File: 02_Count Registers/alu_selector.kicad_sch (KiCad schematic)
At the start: 1 part, among them U11 74LS245

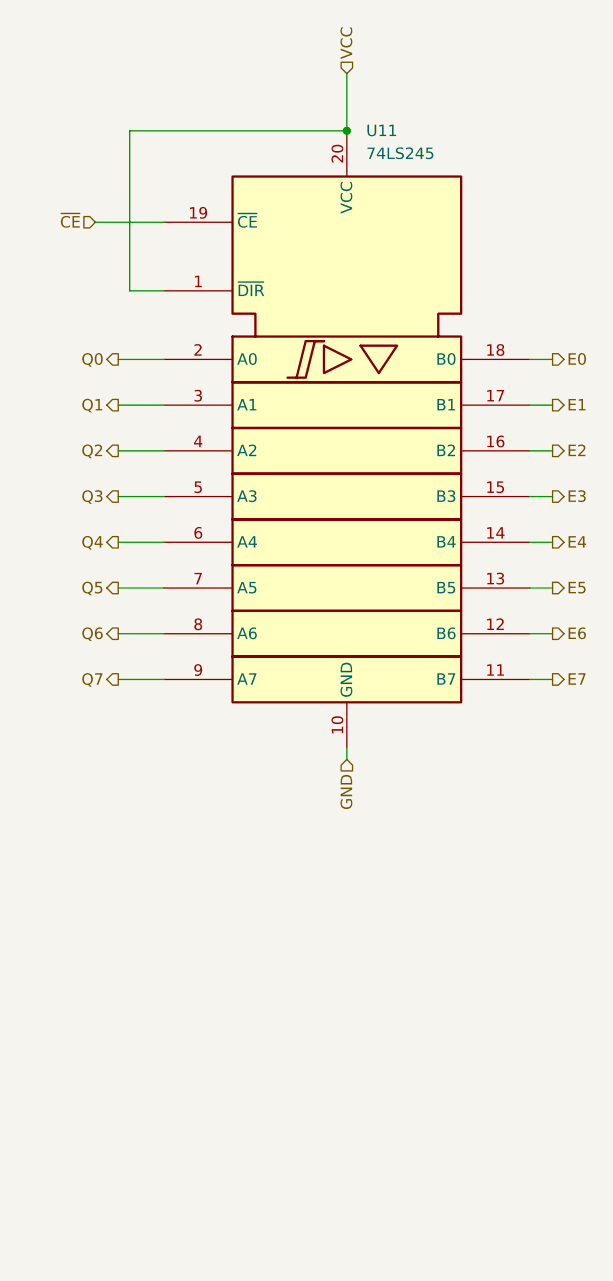
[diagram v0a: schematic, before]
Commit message: Last revision of the cpu, all boards have been ordered. Implementation to be tested and documented in following commits.
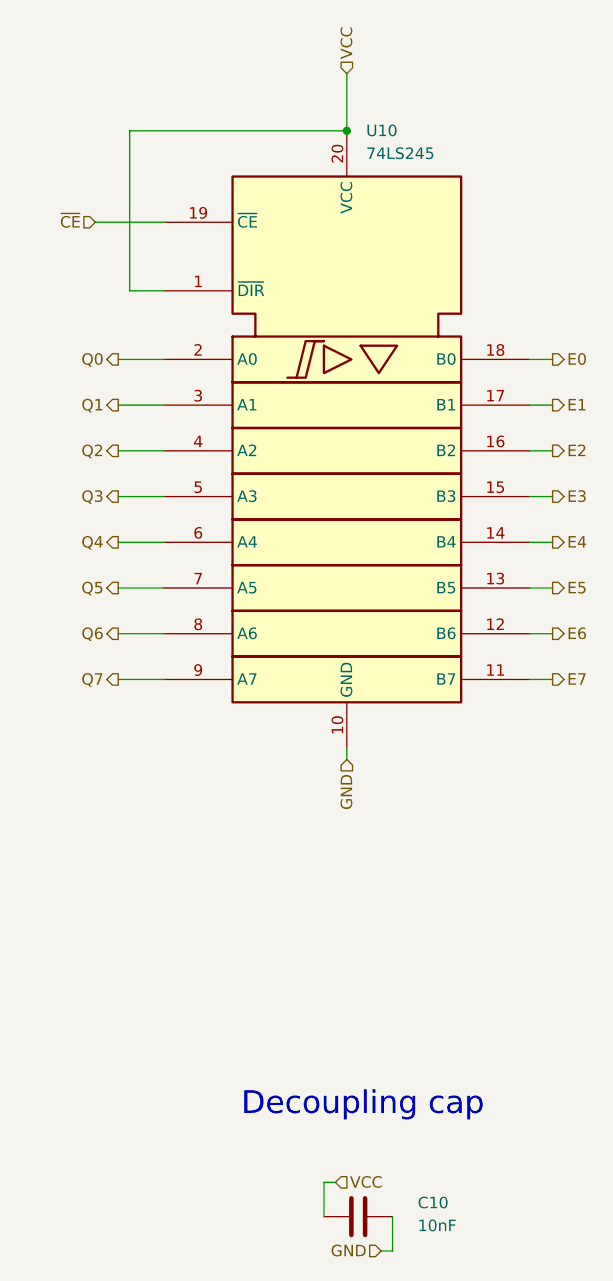
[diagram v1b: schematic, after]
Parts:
- added C10: 10nF, Capacitor_THT:C_Disc_D4.7mm_W2.5mm_P5.00mm, symbol Device:C
- renumbered U11 to U10
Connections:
- net GND: now also C10.2
- net VCC: now also C10.1
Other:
- note added: "Decoupling cap"
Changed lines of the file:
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@@
 		(company "Marco Vettigli")
+	)
+	(text "Decoupling cap"
+		(exclude_from_sim no)
+		(at 156.718 174.244 0)
+		(effects
+			(font
+				(size 2.54 2.54)
+			)
+		)
 	)
 	(junction
@@
 	(wire
 		(pts
+			(xy 160.02 190.5) (xy 160.02 186.69)
+		)
+		(stroke
+			(width 0)
+			(type default)
+		)
+	)
+	(wire
+		(pts
 			(xy 129.54 121.92) (xy 134.62 121.92)
 		)
@@
 	(wire
 		(pts
+			(xy 152.4 182.88) (xy 152.4 186.69)
+		)
+		(stroke
+			(width 0)
+			(type default)
+		)
+	)
+	(wire
+		(pts
 			(xy 129.54 91.44) (xy 134.62 91.44)
 		)
@@
 	(wire
 		(pts
+			(xy 158.75 190.5) (xy 160.02 190.5)
+		)
+		(stroke
+			(width 0)
+			(type default)
+		)
+	)
+	(wire
+		(pts
 			(xy 129.54 101.6) (xy 134.62 101.6)
 		)
@@
 	(wire
 		(pts
+			(xy 153.67 182.88) (xy 152.4 182.88)
+		)
+		(stroke
+			(width 0)
+			(type default)
+		)
+	)
+	(wire
+		(pts
 			(xy 154.94 59.69) (xy 154.94 66.04)
 		)
@@
 		)
 	)
+	(hierarchical_label "VCC"
+		(shape input)
+		(at 153.67 182.88 0)
+		(effects
+			(font
+				(size 1.27 1.27)
+			)
+			(justify left)
+		)
+	)
 	(hierarchical_label "E2"
 		(shape output)
@@
 			)
 			(justify left)
+		)
+	)
+	(hierarchical_label "GND"
+		(shape input)
+		(at 158.75 190.5 180)
+		(effects
+			(font
+				(size 1.27 1.27)
+			)
+			(justify right)
 		)
 	)
@@
 			)
 			(justify left)
+		)
+	)
+	(symbol
+		(lib_id "Device:C")
+		(at 156.21 186.69 90)
+		(unit 1)
+		(exclude_from_sim no)
+		(in_bom yes)
+		(on_board yes)
+		(dnp no)
+		(property "Reference" "C10"
+			(at 162.814 185.166 90)
+			(effects
+				(font
+					(size 1.27 1.27)
+				)
+				(justify right)
+			)
+		)
+		(property "Value" "10nF"
+			(at 162.814 187.706 90)
+			(effects
+				(font
+					(size 1.27 1.27)
+				)
+				(justify right)
+			)
+		)
+		(property "Footprint" "Capacitor_THT:C_Disc_D4.7mm_W2.5mm_P5.00mm"
+			(at 160.02 185.7248 0)
+			(effects
+				(font
+					(size 1.27 1.27)
+				)
+				(hide yes)
+			)
+		)
+		(property "Datasheet" "~"
+			(at 156.21 186.69 0)
+			(effects
+				(font
+					(size 1.27 1.27)
+				)
+				(hide yes)
+			)
+		)
+		(property "Description" "Unpolarized capacitor"
+			(at 156.21 186.69 0)
+			(effects
+				(font
+					(size 1.27 1.27)
+				)
+				(hide yes)
+			)
+		)
+		(pin "2"
+		)
+		(pin "1"
+		)
+		(instances
+			(project "Count Registers"
+				(path "/8a49c3c0-9e79-4a3c-9ae2-67e55d7fae8f/02d723ad-ab13-44db-b1f0-9a59f25d4ef1"
+					(reference "C11")
+					(unit 1)
+				)
+				(path "/8a49c3c0-9e79-4a3c-9ae2-67e55d7fae8f/56373549-06a1-42b1-826c-939e5630208c"
+					(reference "C13")
+					(unit 1)
+				)
+				(path "/8a49c3c0-9e79-4a3c-9ae2-67e55d7fae8f/5f2c1d02-b1c4-49bc-9868-3bf6ba5fa94a"
+					(reference "C12")
+					(unit 1)
+				)
+				(path "/8a49c3c0-9e79-4a3c-9ae2-67e55d7fae8f/d61677ce-7542-4ecf-9e79-3bf6ed766034"
+					(reference "C10")
+					(unit 1)
+				)
+			)
 		)
 	)
@@
 		(dnp no)
 		(fields_autoplaced yes)
-		(property "Reference" "U11"
+		(property "Reference" "U10"
 			(at 157.0833 66.04 0)
 			(effects
@@
 			(project "Count Registers"
 				(path "/8a49c3c0-9e79-4a3c-9ae2-67e55d7fae8f/02d723ad-ab13-44db-b1f0-9a59f25d4ef1"
+					(reference "U11")
+					(unit 1)
+				)
+				(path "/8a49c3c0-9e79-4a3c-9ae2-67e55d7fae8f/56373549-06a1-42b1-826c-939e5630208c"
+					(reference "U13")
+					(unit 1)
+				)
+				(path "/8a49c3c0-9e79-4a3c-9ae2-67e55d7fae8f/5f2c1d02-b1c4-49bc-9868-3bf6ba5fa94a"
 					(reference "U12")
 					(unit 1)
 				)
-				(path "/8a49c3c0-9e79-4a3c-9ae2-67e55d7fae8f/56373549-06a1-42b1-826c-939e5630208c"
-					(reference "U14")
-					(unit 1)
-				)
-				(path "/8a49c3c0-9e79-4a3c-9ae2-67e55d7fae8f/5f2c1d02-b1c4-49bc-9868-3bf6ba5fa94a"
-					(reference "U13")
-					(unit 1)
-				)
 				(path "/8a49c3c0-9e79-4a3c-9ae2-67e55d7fae8f/d61677ce-7542-4ecf-9e79-3bf6ed766034"
-					(reference "U11")
-					(unit 1)
-				)
+					(reference "U10")
+					(unit 1)
+				)
